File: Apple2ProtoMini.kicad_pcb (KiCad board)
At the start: 2 copper layers, 99.8 x 76.4 mm, 3 parts, among them J1 Apple II Bus Card Edge, J2 Apple II Bus Card Pin Header

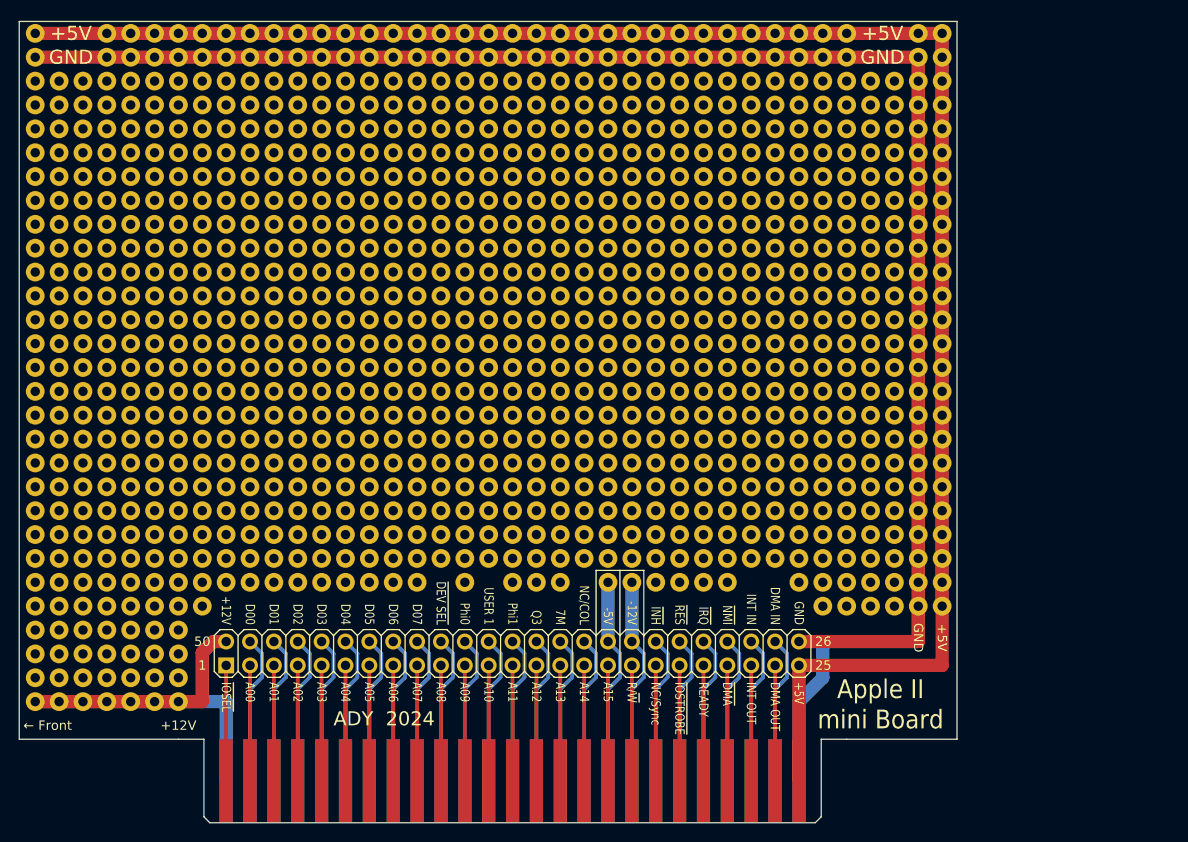
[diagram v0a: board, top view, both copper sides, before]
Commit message: Modify the positions to better match the positions of the full length version.
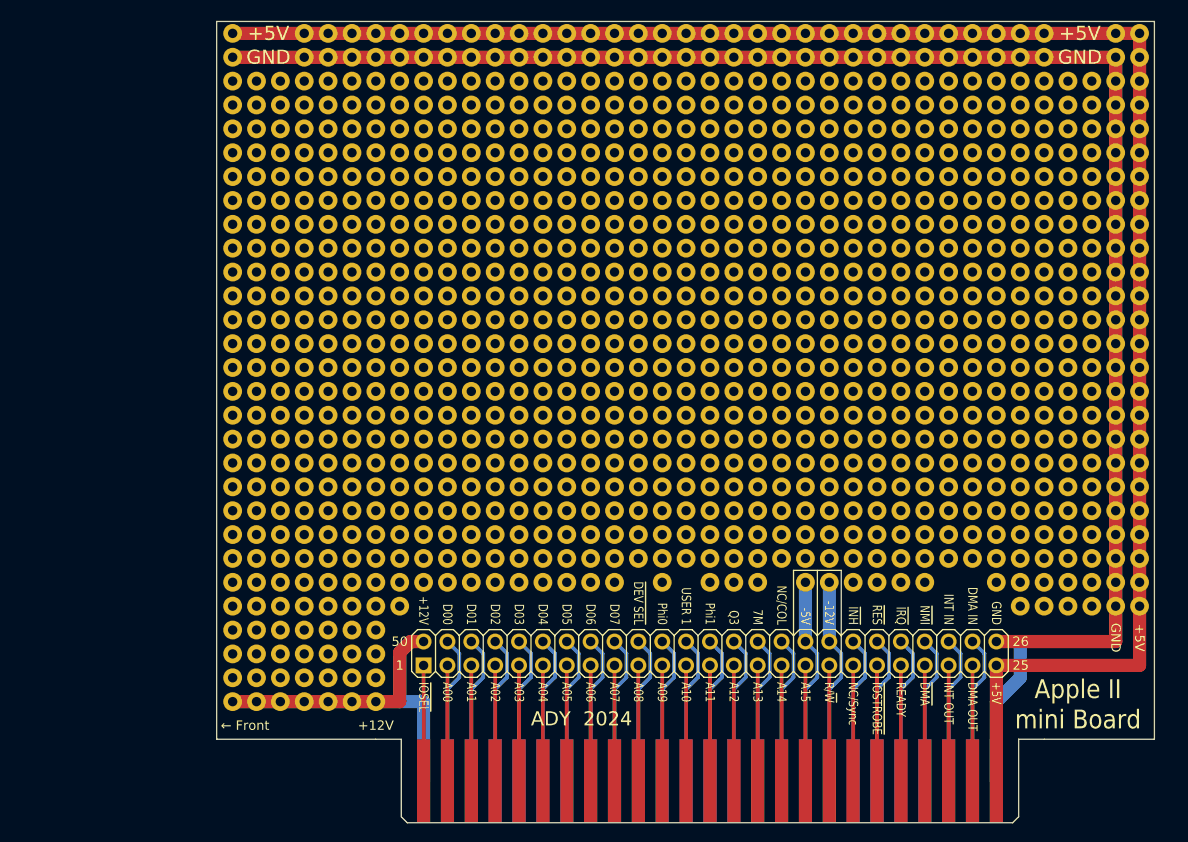
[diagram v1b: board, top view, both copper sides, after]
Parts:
- moved REF** 21.0 mm to (175.9, 128.2)
- moved J1 21.0 mm to (196.2, 136.7)
- moved J2 21.0 mm to (196.2, 124.4)

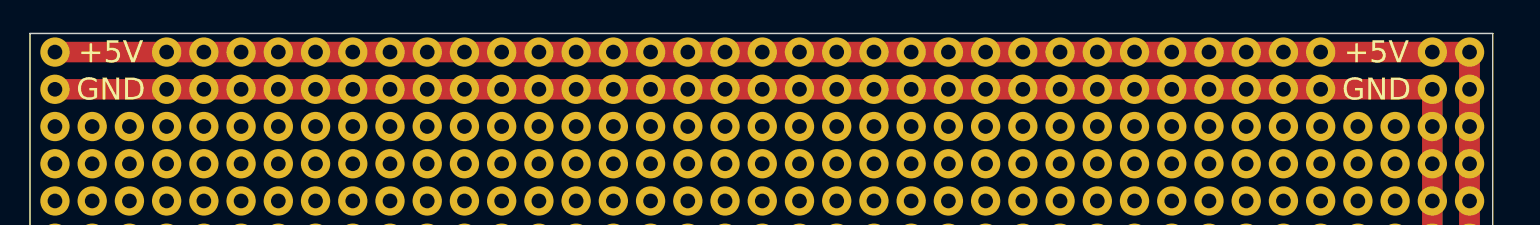
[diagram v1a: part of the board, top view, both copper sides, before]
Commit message: Fixed tying +5V and GND on both sides of the board at the top edge.
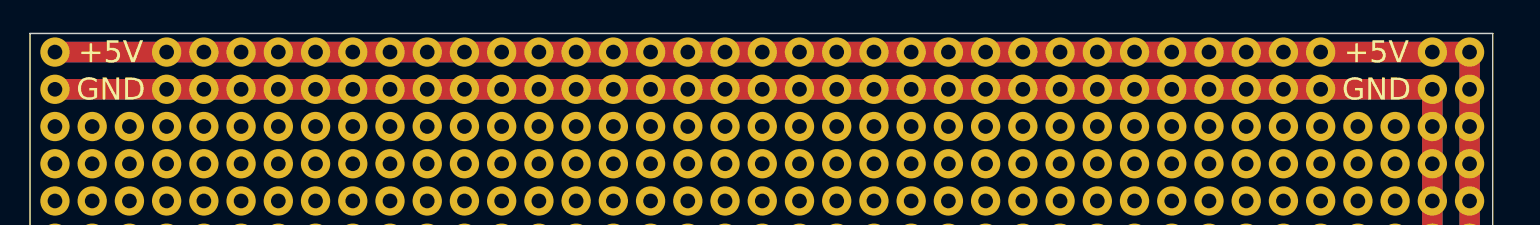
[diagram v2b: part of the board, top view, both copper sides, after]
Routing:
- net +5V: track 252.3 -> 348.8 mm
- net GND: track 259.6 -> 353.6 mm
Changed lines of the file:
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@@
   (segment (start 257.18 124.36) (end 272.42 124.36) (width 1.4) (layer "F.Cu") (net 25))
   (segment (start 272.42 124.36) (end 272.42 57.095) (width 1.4) (layer "F.Cu") (net 25))
-  (segment (start 272.42 57.095) (end 175.9 57.095) (width 1.4) (layer "F.Cu") (net 25))
   (segment (start 257.18 124.36) (end 257.18 136.66) (width 1.4) (layer "F.Cu") (net 25))
+  (segment (start 175.9 57.095) (end 272.42 57.095) (width 1.4) (layer "F.Cu") (net 25))
   (segment (start 272.42 118.055) (end 272.42 57.095) (width 1.4) (layer "B.Cu") (net 25))
+  (segment (start 175.9 57.095) (end 272.42 57.095) (width 1.4) (layer "B.Cu") (net 25))
   (segment (start 269.88 121.82) (end 269.88 59.635) (width 1.4) (layer "F.Cu") (net 26))
   (segment (start 269.88 59.635) (end 175.9 59.635) (width 1.4) (layer "F.Cu") (net 26))
   (segment (start 257.18 121.82) (end 269.88 121.82) (width 1.4) (layer "F.Cu") (net 26))
+  (segment (start 269.88 59.635) (end 175.9 59.635) (width 1.4) (layer "B.Cu") (net 26))
   (segment (start 257.18 128.215) (end 259.72 125.675) (width 1.4) (layer "B.Cu") (net 26))
   (segment (start 259.72 125.675) (end 259.72 121.82) (width 1.4) (layer "B.Cu") (net 26))

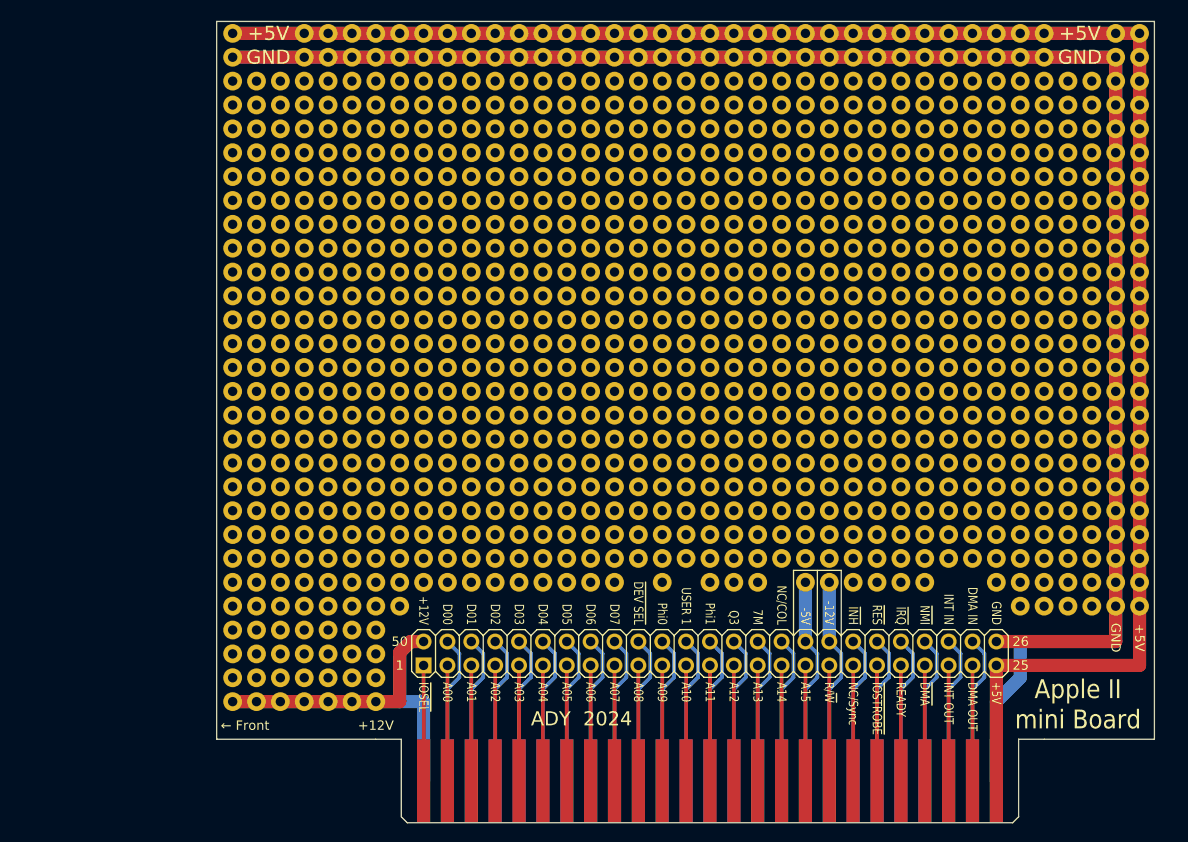
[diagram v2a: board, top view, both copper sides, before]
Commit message: Added Midsized 7" board. Found spec on Apple II Expansion Card sizes (adding to repo). Updated all boards to be within spec (mostly).
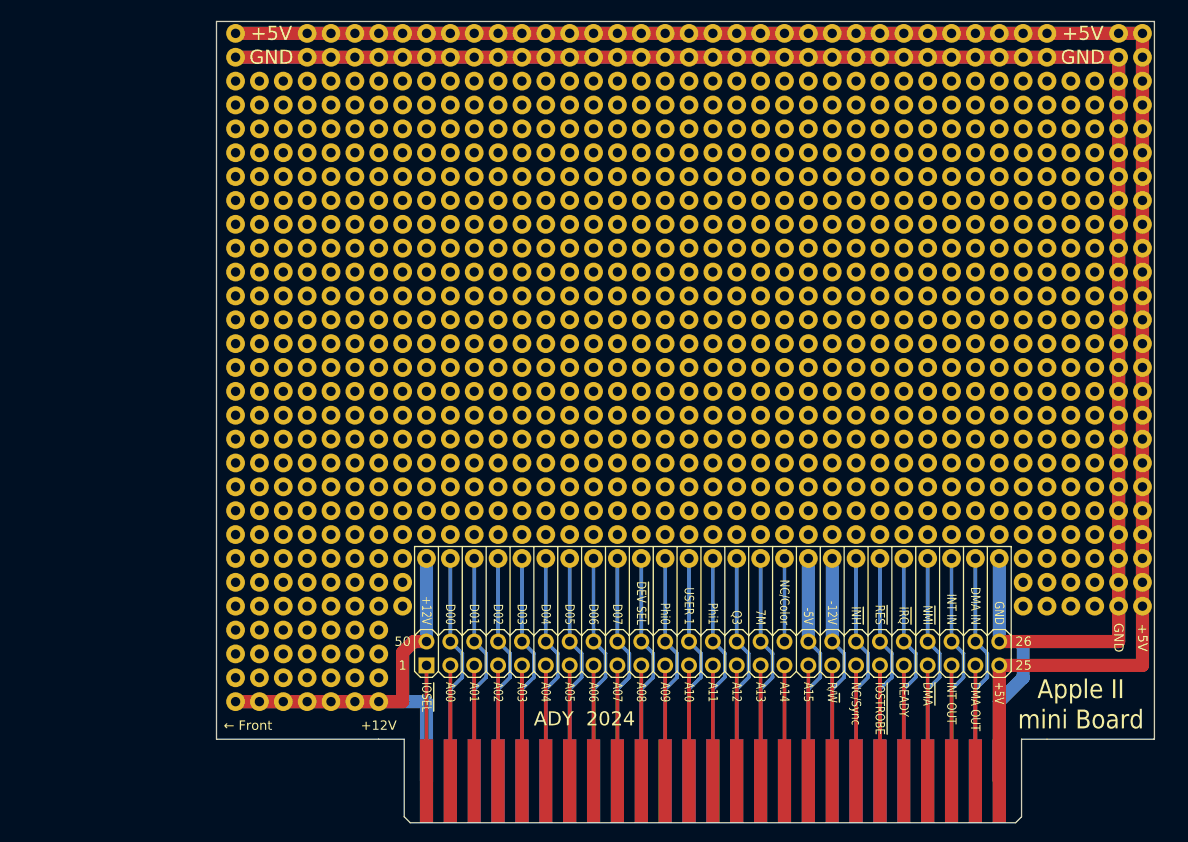
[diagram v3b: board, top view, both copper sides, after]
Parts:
- moved J1 0.31 mm to (196.5, 136.7)
- moved J2 0.31 mm to (196.5, 124.4)
- moved REF** 0.31 mm to (176.2, 128.2)
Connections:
- net /NC/Col renamed /NC/Color
- J1 pad 38: /Phi0 -> /Phi1
- J1 pad 40: /Phi1 -> /Phi0
- J2 pad 38: /Phi0 -> /Phi1
- J2 pad 40: /Phi1 -> /Phi0
- REF** pad : (no net) -> /~{DEVICE_SELECT}
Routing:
- net /Phi1: track 15.9 -> 24.7 mm
- net /DMA_IN: track 15.9 -> 24.7 mm
- net /~{DEVICE_SELECT}: track 15.9 -> 24.7 mm
- net +12V: track 63.0 -> 71.9 mm
- net /D05: track 15.9 -> 24.7 mm
- net /INT_IN: track 15.9 -> 24.7 mm
- net /D06: track 15.9 -> 24.7 mm
- net /D00: track 15.9 -> 24.7 mm
- net /~{RES}: track 15.9 -> 24.7 mm
- net /~{IRQ}: track 15.9 -> 24.7 mm
- net /USER_1: track 15.9 -> 24.7 mm
- net /Q3: track 15.9 -> 24.7 mm
- net /D01: track 15.9 -> 24.7 mm
- net /~{INH}: track 15.9 -> 24.7 mm
- net /D07: track 15.9 -> 24.7 mm
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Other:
- outline, holes or cut-outs redrawn
- board text added: "NC/Color"
- board text removed: "NC/COL"

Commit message: Updated Silk Screen to be easier to read. Added more Apple II documentation.
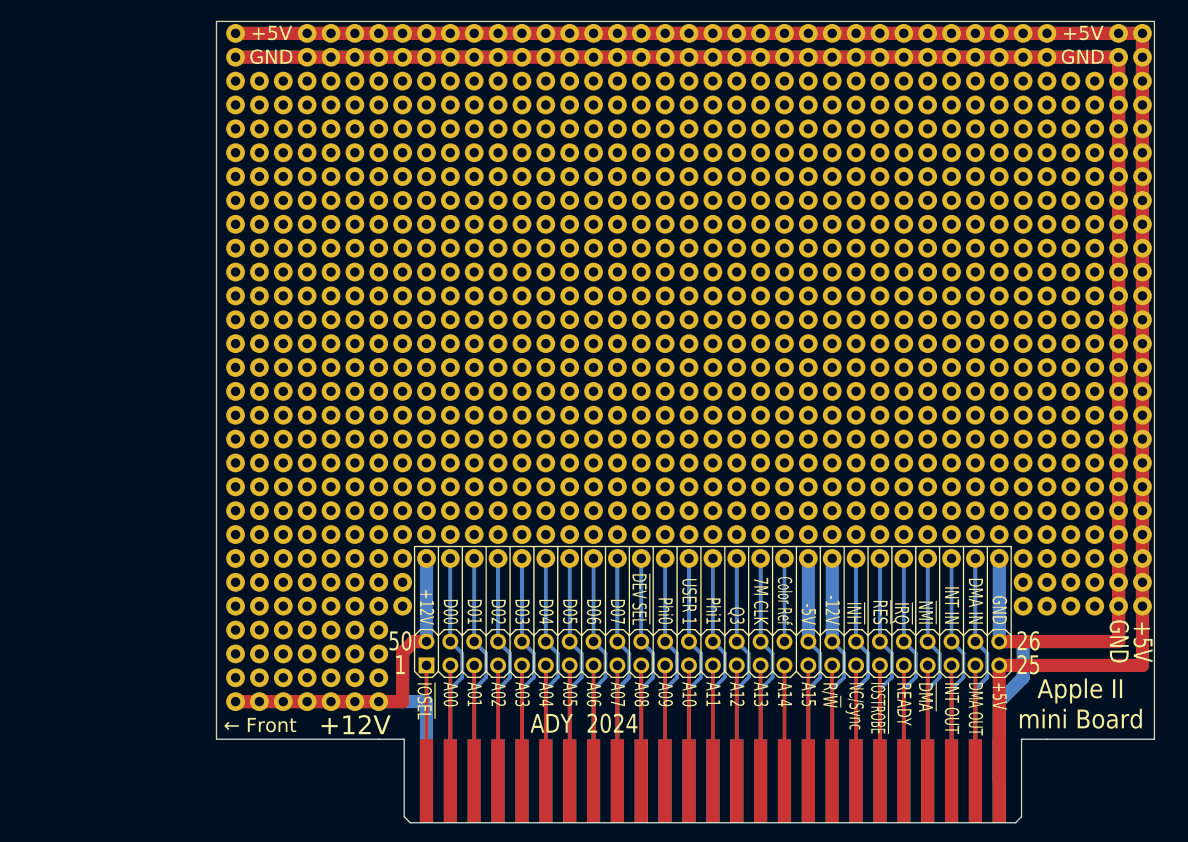
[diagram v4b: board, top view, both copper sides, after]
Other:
- board text added: "7M CLK"
- board text added: "Color Ref"
- board text removed: "7M"
- board text removed: "NC/Color"
